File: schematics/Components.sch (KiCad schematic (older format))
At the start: 10 parts, among them Q1 RFD3055LE, Q2 RFD3055LE, Q3 RFD3055LE, U2 LD1117_3V3

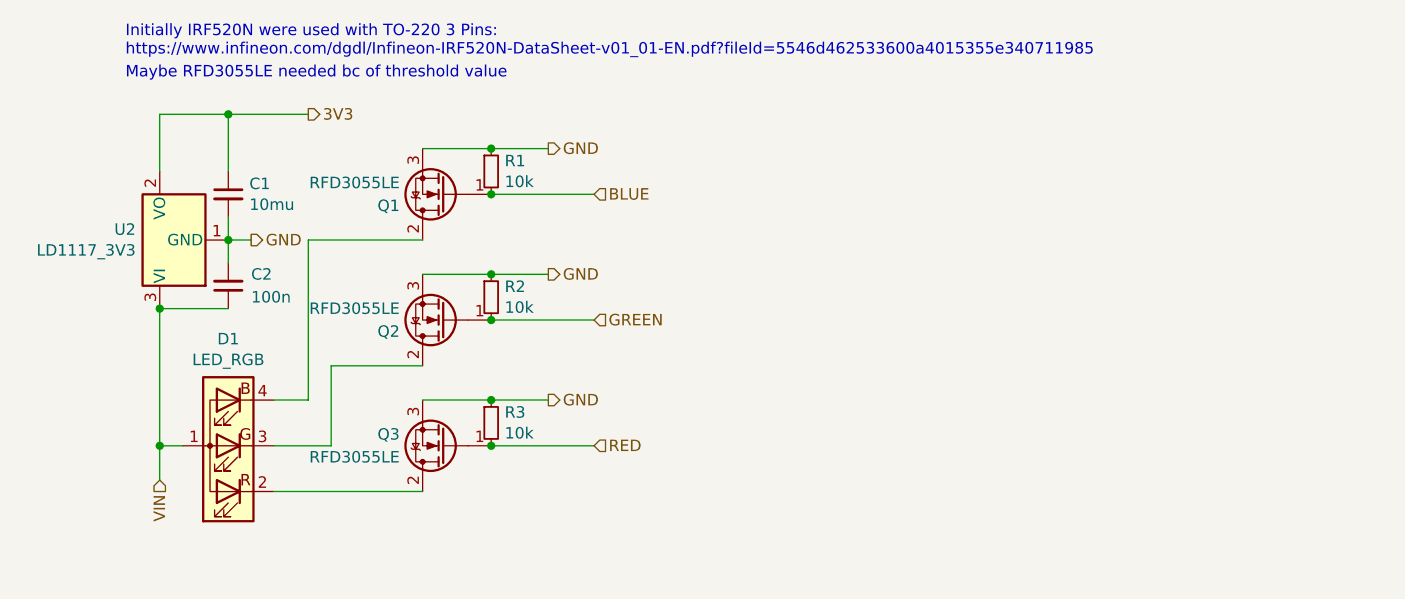
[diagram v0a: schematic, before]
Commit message: Change MOSFET type, rename schematic sheets
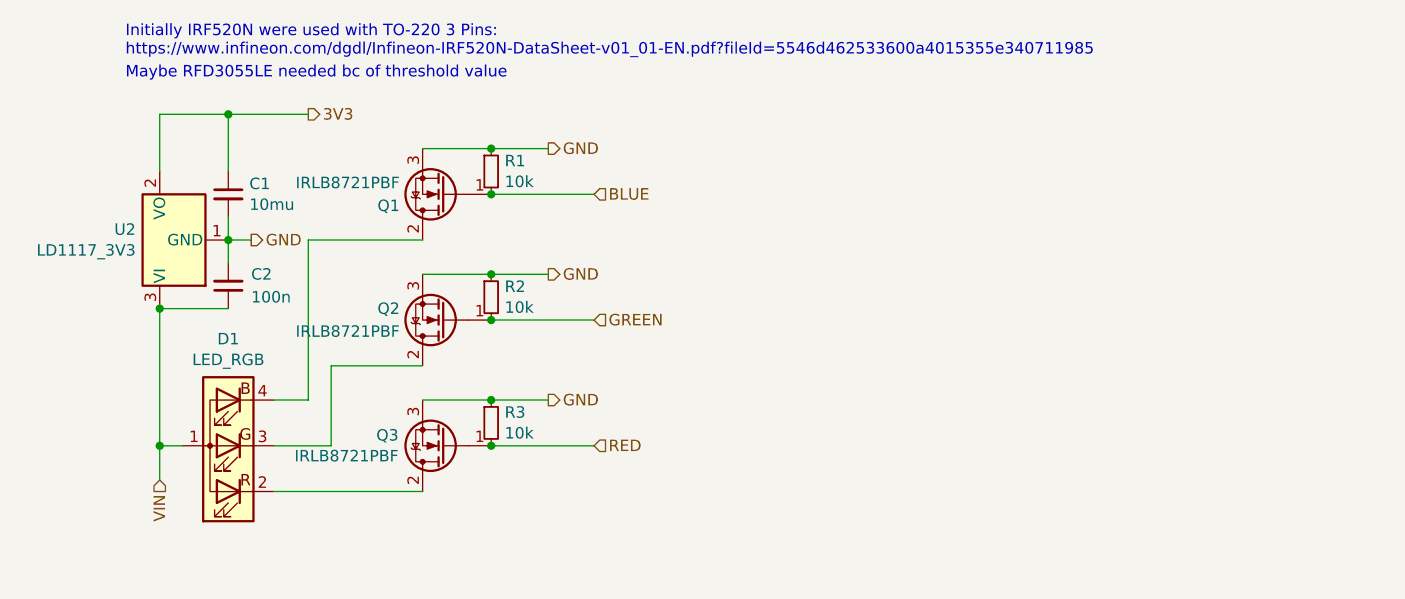
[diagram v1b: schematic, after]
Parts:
- removed Q1, Q2, Q3: RFD3055LE, Package_TO_SOT_THT:TO-251-3_Vertical, symbol Transistor_FET:IRF540N
- added Q1, Q2, Q3: IRLB8721PBF, Package_TO_SOT_THT:TO-220-3_Vertical, symbol Transistor_FET:IRLB8721PBF
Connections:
- net BLUE: now also Q1.1 (G)
- net GND: now also Q1.3 (S), Q2.3 (S), Q3.3 (S)
- net GREEN: now also Q2.1 (G)
- net RED: now also Q3.1 (G)
- net at D1.2 (RK): now also Q3.2 (D)
- net at D1.3 (GK): now also Q2.2 (D)
- net at D1.4 (BK): now also Q1.2 (D)
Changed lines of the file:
@@
 $Descr User 8268 5827
 encoding utf-8
-Sheet 1 2
+Sheet 2 2
 Title "Generic RGB LED strip controller"
 Date ""
@@
 	0    -1   -1   0
 $EndComp
-$Comp
-L Transistor_FET:IRF540N Q2
-U 1 1 60F03EB6
-P 3750 2850
-F 0 "Q2" H 3950 2900 50  0000 L CNN
-F 1 "RFD3055LE" H 3950 2800 50  0000 L CNN
-F 2 "Package_TO_SOT_THT:TO-251-3_Vertical" H 4000 2775 50  0001 L CIN
-F 3 "https://www.mouser.com/datasheet/2/308/1/RFD3055LESM_D-2319857.pdf" H 3750 2850 50  0001 L CNN
-	1    3750 2850
-	-1   0    0    1
-$EndComp
-$Comp
-L Transistor_FET:IRF540N Q1
-U 1 1 60F0615A
-P 3750 2300
-F 0 "Q1" H 3950 2350 50  0000 L CNN
-F 1 "RFD3055LE" H 3950 2250 50  0000 L CNN
-F 2 "Package_TO_SOT_THT:TO-251-3_Vertical" H 4000 2225 50  0001 L CIN
-F 3 "https://www.mouser.com/datasheet/2/308/1/RFD3055LESM_D-2319857.pdf" H 3750 2300 50  0001 L CNN
-	1    3750 2300
-	-1   0    0    1
-$EndComp
 Wire Wire Line
 	3650 3600 3000 3600
@@
 3V3
 $Comp
-L Transistor_FET:IRF540N Q3
-U 1 1 60F024FB
+L Transistor_FET:IRLB8721PBF Q1
+U 1 1 60FA2BCA
+P 3750 2300
+F 0 "Q1" H 3950 2350 50  0000 L CNN
+F 1 "IRLB8721PBF" H 3950 2250 50  0000 L CNN
+F 2 "Package_TO_SOT_THT:TO-220-3_Vertical" H 4000 2225 50  0001 L CIN
+F 3 "http://www.infineon.com/dgdl/irlb8721pbf.pdf?fileId=5546d462533600a40153566056732591" H 3750 2300 50  0001 L CNN
+	1    3750 2300
+	-1   0    0    1
+$EndComp
+$Comp
+L Transistor_FET:IRLB8721PBF Q2
+U 1 1 60FA8D3E
+P 3750 2850
+F 0 "Q2" H 3950 2800 50  0000 L CNN
+F 1 "IRLB8721PBF" H 3950 2900 50  0000 L CNN
+F 2 "Package_TO_SOT_THT:TO-220-3_Vertical" H 4000 2775 50  0001 L CIN
+F 3 "http://www.infineon.com/dgdl/irlb8721pbf.pdf?fileId=5546d462533600a40153566056732591" H 3750 2850 50  0001 L CNN
+	1    3750 2850
+	-1   0    0    1
+$EndComp
+$Comp
+L Transistor_FET:IRLB8721PBF Q3
+U 1 1 60FA9F10
 P 3750 3400
-F 0 "Q3" H 3950 3350 50  0000 L CNN
-F 1 "RFD3055LE" H 3950 3450 50  0000 L CNN
-F 2 "Package_TO_SOT_THT:TO-251-3_Vertical" H 4000 3325 50  0001 L CIN
-F 3 "https://www.mouser.com/datasheet/2/308/1/RFD3055LESM_D-2319857.pdf" H 3750 3400 50  0001 L CNN
+F 0 "Q3" H 3955 3354 50  0000 L CNN
+F 1 "IRLB8721PBF" H 3955 3445 50  0000 L CNN
+F 2 "Package_TO_SOT_THT:TO-220-3_Vertical" H 4000 3325 50  0001 L CIN
+F 3 "http://www.infineon.com/dgdl/irlb8721pbf.pdf?fileId=5546d462533600a40153566056732591" H 3750 3400 50  0001 L CNN
 	1    3750 3400
 	-1   0    0    1

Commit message: Change LED from RGB to GRB
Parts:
- removed D1: LED_RGB, Connector_PinHeader_2.54mm:PinHeader_1x04_P2.54mm_Vertical, symbol Device:LED_ARGB
- added D1: LED_AGRB, symbol Device:LED_AGRB
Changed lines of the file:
@@
 	2800 2500 2800 2600
 Connection ~ 2800 2500
-$Comp
-L Device:LED_ARGB D1
-U 1 1 60F08554
-P 2800 3400
-F 0 "D1" H 2800 2933 50  0000 C CNN
-F 1 "LED_RGB" H 2800 3024 50  0000 C CNN
-F 2 "Connector_PinHeader_2.54mm:PinHeader_1x04_P2.54mm_Vertical" H 2800 3350 50  0001 C CNN
-F 3 "~" H 2800 3350 50  0001 C CNN
-	1    2800 3400
-	-1   0    0    1
-$EndComp
 Text HLabel 4400 3400 2    50   Input ~ 0
 RED
@@
 	-1   0    0    1
 $EndComp
+$Comp
+L Device:LED_AGRB D1
+U 1 1 60FB361C
+P 2800 3400
+F 0 "D1" H 2800 2933 50  0000 C CNN
+F 1 "LED_AGRB" H 2800 3024 50  0000 C CNN
+F 2 "" H 2800 3350 50  0001 C CNN
+F 3 "~" H 2800 3350 50  0001 C CNN
+	1    2800 3400
+	-1   0    0    1
+$EndComp

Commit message: Change capacitors to elkos
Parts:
- removed C1: 10mu, Capacitor_THT:CP_Radial_D6.3mm_P2.50mm, symbol Device:C_Small
- removed C2: 100n, Capacitor_THT:C_Disc_D7.0mm_W2.5mm_P5.00mm, symbol Device:C_Small
- added C1: 10u, symbol Device:CP_Small
- added C2: 100n, symbol Device:CP_Small
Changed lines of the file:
@@
 Wire Wire Line
 	2500 1950 2800 1950
-$Comp
-L Device:C_Small C1
-U 1 1 60F33F39
-P 2800 2300
-F 0 "C1" H 2892 2346 50  0000 L CNN
-F 1 "10mu" H 2892 2255 50  0000 L CNN
-F 2 "Capacitor_THT:CP_Radial_D6.3mm_P2.50mm" H 2800 2300 50  0001 C CNN
-F 3 "~" H 2800 2300 50  0001 C CNN
-	1    2800 2300
-	1    0    0    -1
-$EndComp
-$Comp
-L Device:C_Small C2
-U 1 1 60F35104
-P 2800 2700
-F 0 "C2" H 2700 2650 50  0000 R CNN
-F 1 "100n" H 2700 2750 50  0000 R CNN
-F 2 "Capacitor_THT:C_Disc_D7.0mm_W2.5mm_P5.00mm" H 2800 2700 50  0001 C CNN
-F 3 "~" H 2800 2700 50  0001 C CNN
-	1    2800 2700
-	-1   0    0    1
-$EndComp
 Wire Wire Line
 	2800 2200 2800 1950
@@
 	-1   0    0    1
 $EndComp
+$Comp
+L Device:CP_Small C1
+U 1 1 60FC326D
+P 2800 2300
+F 0 "C1" H 2712 2254 50  0000 R CNN
+F 1 "10u" H 2712 2345 50  0000 R CNN
+F 2 "" H 2800 2300 50  0001 C CNN
+F 3 "~" H 2800 2300 50  0001 C CNN
+	1    2800 2300
+	-1   0    0    1
+$EndComp
+$Comp
+L Device:CP_Small C2
+U 1 1 60FC4AE6
+P 2800 2700
+F 0 "C2" H 2712 2654 50  0000 R CNN
+F 1 "100n" H 2712 2745 50  0000 R CNN
+F 2 "" H 2800 2700 50  0001 C CNN
+F 3 "~" H 2800 2700 50  0001 C CNN
+	1    2800 2700
+	-1   0    0    1
+$EndComp
